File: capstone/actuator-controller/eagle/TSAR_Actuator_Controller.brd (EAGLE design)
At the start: 160 x 100 mm, 0 parts

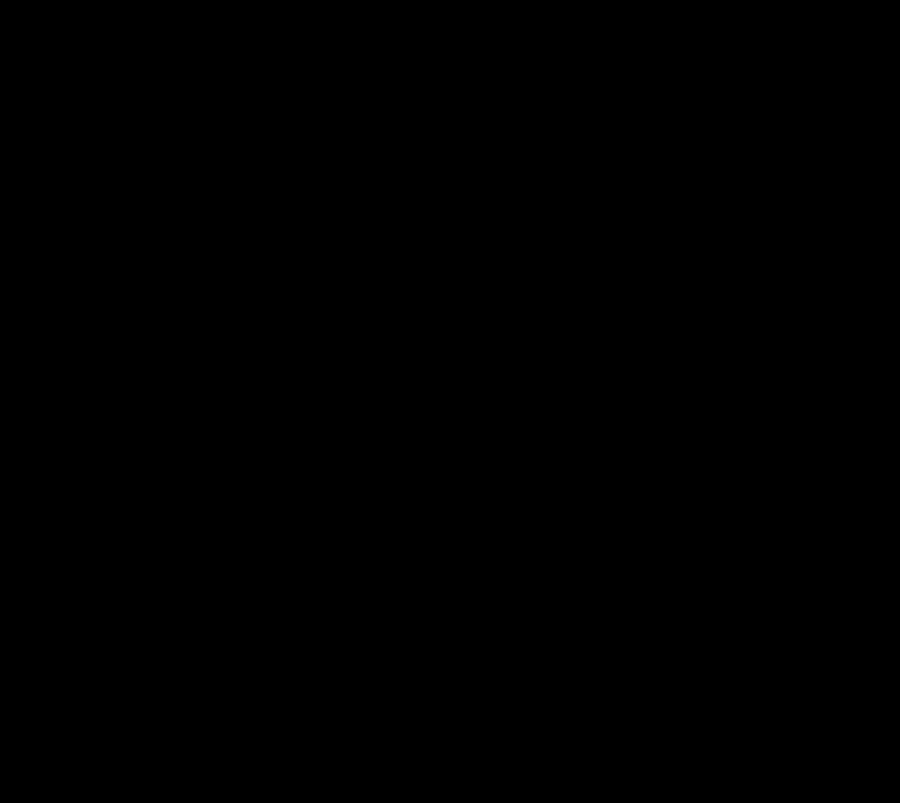
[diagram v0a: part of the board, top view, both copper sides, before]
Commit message: FW: Added binaries, fixed some HAL options. HW: Created STM32 footprint/drawing.
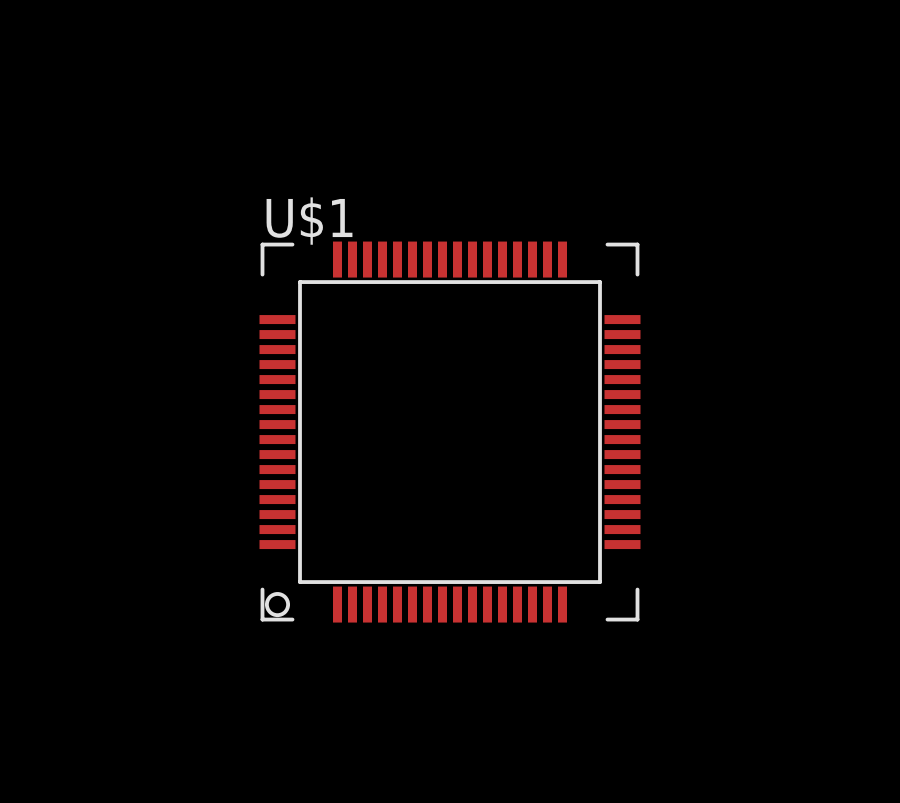
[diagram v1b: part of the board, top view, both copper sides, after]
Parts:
- added U$1: STM32GO71, TSAR_Controller:LQFP64
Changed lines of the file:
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@@
 <?xml version="1.0" encoding="utf-8"?>
 <!DOCTYPE eagle SYSTEM "eagle.dtd">
-<eagle version="9.4.2">
+<eagle version="9.5.1">
 <drawing>
 <settings>
@@
 </autorouter>
 <elements>
+<element name="U$1" library="TSAR_Controller" package="LQFP64" value="STM32GO71" x="26.67" y="33.02" smashed="yes">
+<attribute name="NAME" x="20.42" y="39.52" size="1.27" layer="25"/>
+<attribute name="VALUE" x="20.67" y="25.02" size="1.27" layer="27"/>
+</element>
 </elements>
 <signals>
